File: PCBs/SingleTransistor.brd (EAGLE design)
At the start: 16 x 33 mm, 4 parts, among them T1 BC547N

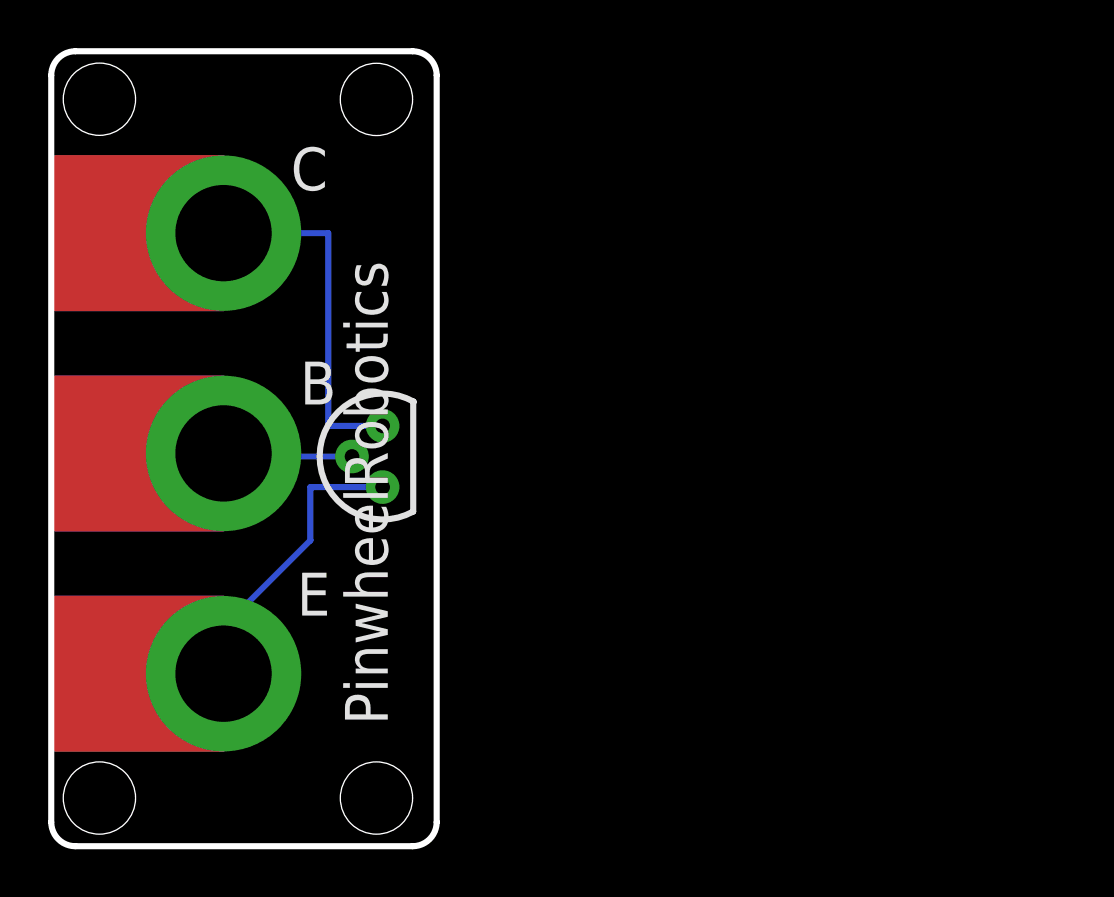
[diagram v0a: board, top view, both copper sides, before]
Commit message: Update for Dim width is 42 length is 28 for type 2 pcb
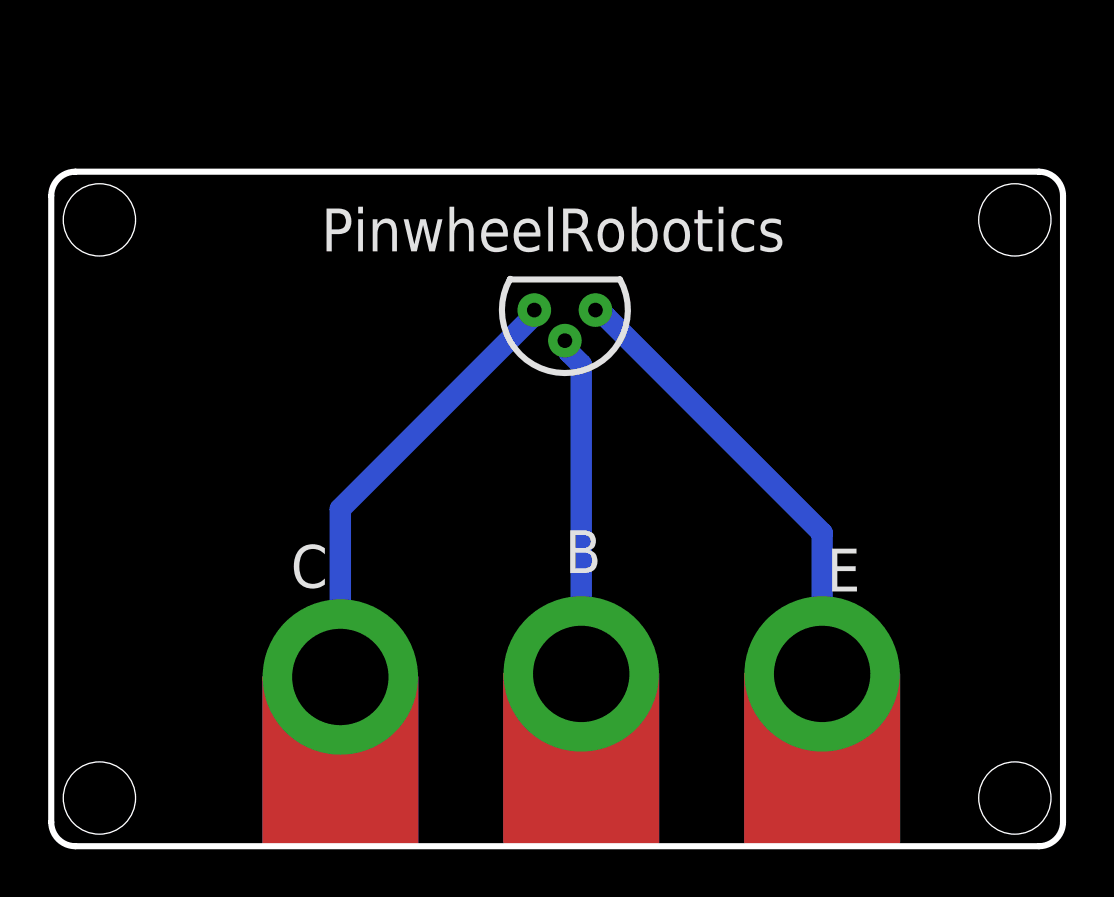
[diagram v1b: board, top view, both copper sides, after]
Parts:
- moved U$3 24.8 mm to (32.0, 7.15), turned to 0 degrees
- moved U$1 19.1 mm to (12.0, 7.03), turned to 0 degrees
- moved U$2 17.4 mm to (22.0, 7.15), turned to 0 degrees
- moved T1 11.5 mm to (22.6, 22.3), turned to 180 degrees
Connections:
- net N$2 renamed T1
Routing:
- net T1: track 5.46 -> 14.1 mm
- net N$1: track 12.7 -> 19.1 mm
- net N$3: track 14.6 -> 18.5 mm
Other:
- board size 16 x 33 mm -> 42 x 28 mm
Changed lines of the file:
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@@
 <drawing>
 <settings>
-<setting alwaysvectorfont="no"/>
+<setting alwaysvectorfont="yes"/>
 <setting verticaltext="up"/>
 </settings>
@@
 <layer number="45" name="Holes" color="7" fill="1" visible="yes" active="yes"/>
 <layer number="46" name="Milling" color="3" fill="1" visible="no" active="yes"/>
-<layer number="47" name="Measures" color="7" fill="1" visible="no" active="yes"/>
+<layer number="47" name="Measures" color="7" fill="1" visible="yes" active="yes"/>
 <layer number="48" name="Document" color="7" fill="1" visible="yes" active="yes"/>
 <layer number="49" name="Reference" color="7" fill="1" visible="yes" active="yes"/>
@@
 <board>
 <plain>
-<text x="10.2" y="9.574" size="1.778" layer="21">E</text>
-<text x="10.327" y="18.337" size="1.778" layer="21">B</text>
-<text x="9.946" y="27.227" size="1.778" layer="21">C</text>
-<hole x="2" y="31.008" drill="3"/>
-<hole x="13.5" y="31" drill="3"/>
-<hole x="13.5" y="2" drill="3"/>
+<text x="32.2" y="10.574" size="1.778" layer="21">E</text>
+<text x="21.327" y="11.337" size="1.778" layer="21">B</text>
+<text x="9.946" y="10.727" size="1.778" layer="21">C</text>
+<hole x="2" y="26" drill="3"/>
+<hole x="40" y="26" drill="3"/>
+<hole x="40" y="2" drill="3"/>
 <hole x="2" y="2" drill="3"/>
-<text x="13.971" y="5.042" size="1.778" layer="21" rot="R90">PinwheelRobotics</text>
-<text x="4.471" y="25.465" size="1.778" layer="22" rot="MR270">care@pinwheel.in</text>
-<wire x1="0" y1="1" x2="0" y2="32" width="0.254" layer="20"/>
-<wire x1="0" y1="32" x2="1" y2="33" width="0.254" layer="20" curve="-90"/>
-<wire x1="1" y1="33" x2="15" y2="33" width="0.254" layer="20"/>
-<wire x1="15" y1="33" x2="16" y2="32" width="0.254" layer="20" curve="-90"/>
-<wire x1="16" y1="32" x2="16" y2="1" width="0.254" layer="20"/>
-<wire x1="16" y1="1" x2="15" y2="0" width="0.254" layer="20" curve="-90"/>
-<wire x1="15" y1="0" x2="1" y2="0" width="0.254" layer="20"/>
+<text x="30.458" y="26.471" size="1.778" layer="21" rot="R180">PinwheelRobotics</text>
+<text x="10.535" y="26.471" size="1.778" layer="22" rot="MR180">care@pinwheel.in</text>
+<wire x1="42" y1="27" x2="42" y2="1" width="0.254" layer="20"/>
+<wire x1="42" y1="1" x2="41" y2="0" width="0.254" layer="20" curve="-90"/>
+<wire x1="41" y1="0" x2="1" y2="0" width="0.254" layer="20"/>
 <wire x1="1" y1="0" x2="0" y2="1" width="0.254" layer="20" curve="-90"/>
-<dimension x1="-1.5" y1="33" x2="-1.5" y2="0" x3="-2.5" y3="16.5" textsize="1.778" layer="1"/>
-<dimension x1="0" y1="33.5" x2="16" y2="33.5" x3="8" y3="35.5" textsize="1.778" layer="1"/>
+<wire x1="0" y1="1" x2="0" y2="27" width="0.254" layer="20"/>
+<wire x1="0" y1="27" x2="1" y2="28" width="0.254" layer="20" curve="-90"/>
+<wire x1="1" y1="28" x2="41" y2="28" width="0.254" layer="20"/>
+<wire x1="41" y1="28" x2="42" y2="27" width="0.254" layer="20" curve="-90"/>
 </plain>
 <attributes>
@@
 </class>
 </classes>
-<designrules name="default">
+<designrules name="default *">
 <description language="de">&lt;b&gt;EAGLE Design Rules&lt;/b&gt;
 &lt;p&gt;
@@
 <param name="mdDrill" value="6mil"/>
 <param name="mdSmdStop" value="0mil"/>
-<param name="msWidth" value="6mil"/>
+<param name="msWidth" value="35mil"/>
 <param name="msDrill" value="0.35mm"/>
 <param name="msMicroVia" value="9.99mm"/>
@@
 <param name="TopRouterVariant" value="1"/>
 <param name="tpViaShape" value="round"/>
-<param name="PrefDir.1" value="0"/>
+<param name="PrefDir.1" value="a"/>
 <param name="PrefDir.2" value="0"/>
 <param name="PrefDir.3" value="0"/>
@@
 </autorouter>
 <elements>
-<element name="T1" library="BC547" package="TO92" value="BC547N" x="13.756" y="14.908" smashed="yes" rot="R90">
-<attribute name="AVAILABILITY" value="In Stock" x="16.296" y="37.768" size="1.778" layer="27" rot="R90" display="off"/>
-<attribute name="CHECK_PRICES" value="https://www.snapeda.com/parts/BC547/Onsemi/view-part/?ref=eda" x="16.296" y="37.768" size="1.778" layer="27" rot="R90" display="off"/>
-<attribute name="DESCRIPTION" value=" Trans GP BJT NPN 45V 0.1A 500mW 3-Pin TO-92 T/R " x="16.296" y="37.768" size="1.778" layer="27" rot="R90" display="off"/>
-<attribute name="MF" value="ON Semiconductor" x="16.296" y="37.768" size="1.778" layer="27" rot="R90" display="off"/>
-<attribute name="MP" value="BC547" x="16.296" y="37.768" size="1.778" layer="27" rot="R90" display="off"/>
-<attribute name="PACKAGE" value="None" x="16.296" y="37.768" size="1.778" layer="27" rot="R90" display="off"/>
-<attribute name="PRICE" value="None" x="16.296" y="37.768" size="1.778" layer="27" rot="R90" display="off"/>
-<attribute name="PURCHASE-URL" value="https://www.snapeda.com/api/url_track_click_mouser/?unipart_id=11254981&amp;manufacturer=ON Semiconductor&amp;part_name=BC547&amp;search_term=None" x="16.296" y="37.768" size="1.778" layer="27" rot="R90" display="off"/>
-<attribute name="SNAPEDA_LINK" value="https://www.snapeda.com/parts/BC547/Onsemi/view-part/?ref=snap" x="16.296" y="37.768" size="1.778" layer="27" rot="R90" display="off"/>
-<attribute name="VALUE" x="10.962" y="18.337" size="0.8128" layer="27" rot="R270"/>
+<element name="T1" library="BC547" package="TO92" value="BC547N" x="22.592" y="22.256" smashed="yes" rot="R180">
+<attribute name="AVAILABILITY" value="In Stock" x="-0.268" y="24.796" size="1.778" layer="27" rot="R180" display="off"/>
+<attribute name="CHECK_PRICES" value="https://www.snapeda.com/parts/BC547/Onsemi/view-part/?ref=eda" x="-0.268" y="24.796" size="1.778" layer="27" rot="R180" display="off"/>
+<attribute name="DESCRIPTION" value=" Trans GP BJT NPN 45V 0.1A 500mW 3-Pin TO-92 T/R " x="-0.268" y="24.796" size="1.778" layer="27" rot="R180" display="off"/>
+<attribute name="MF" value="ON Semiconductor" x="-0.268" y="24.796" size="1.778" layer="27" rot="R180" display="off"/>
+<attribute name="MP" value="BC547" x="-0.268" y="24.796" size="1.778" layer="27" rot="R180" display="off"/>
+<attribute name="PACKAGE" value="None" x="-0.268" y="24.796" size="1.778" layer="27" rot="R180" display="off"/>
+<attribute name="PRICE" value="None" x="-0.268" y="24.796" size="1.778" layer="27" rot="R180" display="off"/>
+<attribute name="PURCHASE-URL" value="https://www.snapeda.com/api/url_track_click_mouser/?unipart_id=11254981&amp;manufacturer=ON Semiconductor&amp;part_name=BC547&amp;search_term=None" x="-0.268" y="24.796" size="1.778" layer="27" rot="R180" display="off"/>
+<attribute name="SNAPEDA_LINK" value="https://www.snapeda.com/parts/BC547/Onsemi/view-part/?ref=snap" x="-0.268" y="24.796" size="1.778" layer="27" rot="R180" display="off"/>
+<attribute name="VALUE" x="19.663" y="18.462" size="0.8128" layer="27"/>
 </element>
-<element name="U$1" library="microbit" package="MICROBIT_PAD" value="MICROBIT_PAD" x="7.152" y="25.449" smashed="yes" rot="R270"/>
-<element name="U$2" library="microbit" package="MICROBIT_PAD" value="MICROBIT_PAD" x="7.152" y="16.305" smashed="yes" rot="R270"/>
-<element name="U$3" library="microbit" package="MICROBIT_PAD" value="MICROBIT_PAD" x="7.152" y="7.161" smashed="yes" rot="R270"/>
+<element name="U$1" library="microbit" package="MICROBIT_PAD" value="MICROBIT_PAD" x="12" y="7.025" smashed="yes"/>
+<element name="U$2" library="microbit" package="MICROBIT_PAD" value="MICROBIT_PAD" x="22" y="7.152" smashed="yes"/>
+<element name="U$3" library="microbit" package="MICROBIT_PAD" value="MICROBIT_PAD" x="32" y="7.152" smashed="yes"/>
 </elements>
 <signals>
@@
 <contactref element="U$3" pad="PAD"/>
 <contactref element="T1" pad="1"/>
-<wire x1="13.756" y1="14.908" x2="10.7588" y2="14.908" width="0.254" layer="16"/>
-<wire x1="7.152" y1="9.8661" x2="7.152" y2="7.161" width="0.254" layer="16"/>
-<wire x1="10.7588" y1="14.908" x2="10.7588" y2="12.6982" width="0.254" layer="16"/>
-<wire x1="10.7588" y1="12.6982" x2="7.9267" y2="9.8661" width="0.254" layer="16"/>
-<wire x1="7.9267" y1="9.8661" x2="7.152" y2="9.8661" width="0.254" layer="16"/>
+<wire x1="32" y1="13" x2="23" y2="22" width="0.889" layer="16"/>
+<wire x1="32" y1="7.152" x2="32" y2="13" width="0.889" layer="16"/>
+<wire x1="23" y1="22" x2="22.592" y2="22.256" width="0.889" layer="16"/>
 </signal>
-<signal name="N$2">
+<signal name="T1">
 <contactref element="T1" pad="2"/>
 <contactref element="U$2" pad="PAD"/>
-<wire x1="12.486" y1="16.178" x2="7.152" y2="16.178" width="0.254" layer="16"/>
-<wire x1="7.152" y1="16.178" x2="7.152" y2="16.305" width="0.254" layer="16"/>
+<wire x1="22" y1="20" x2="21.5" y2="20.5" width="0.889" layer="16"/>
+<wire x1="22" y1="7.152" x2="22" y2="20" width="0.889" layer="16"/>
+<wire x1="21.5" y1="20.5" x2="21.322" y2="20.986" width="0.889" layer="16"/>
 </signal>
 <signal name="N$3">
 <contactref element="T1" pad="3"/>
 <contactref element="U$1" pad="PAD"/>
-<wire x1="7.152" y1="25.449" x2="11.5" y2="25.449" width="0.254" layer="16"/>
-<wire x1="11.5" y1="17.448" x2="13.756" y2="17.448" width="0.254" layer="16"/>
-<wire x1="11.5" y1="25.449" x2="11.5" y2="17.448" width="0.254" layer="16"/>
+<wire x1="12" y1="14" x2="20" y2="22" width="0.889" layer="16"/>
+<wire x1="12" y1="7.025" x2="12" y2="14" width="0.889" layer="16"/>
+<wire x1="20" y1="22" x2="20.052" y2="22.256" width="0.889" layer="16"/>
 </signal>
 </signals>
@@
 <mfgpreviewcolor name="substratecolor" color="0xFF786E46"/>
 </mfgpreviewcolors>
-<errors>
-</errors>
 </board>
 </drawing>

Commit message: Corrected hole position for some design , made transistor as switch as category 1
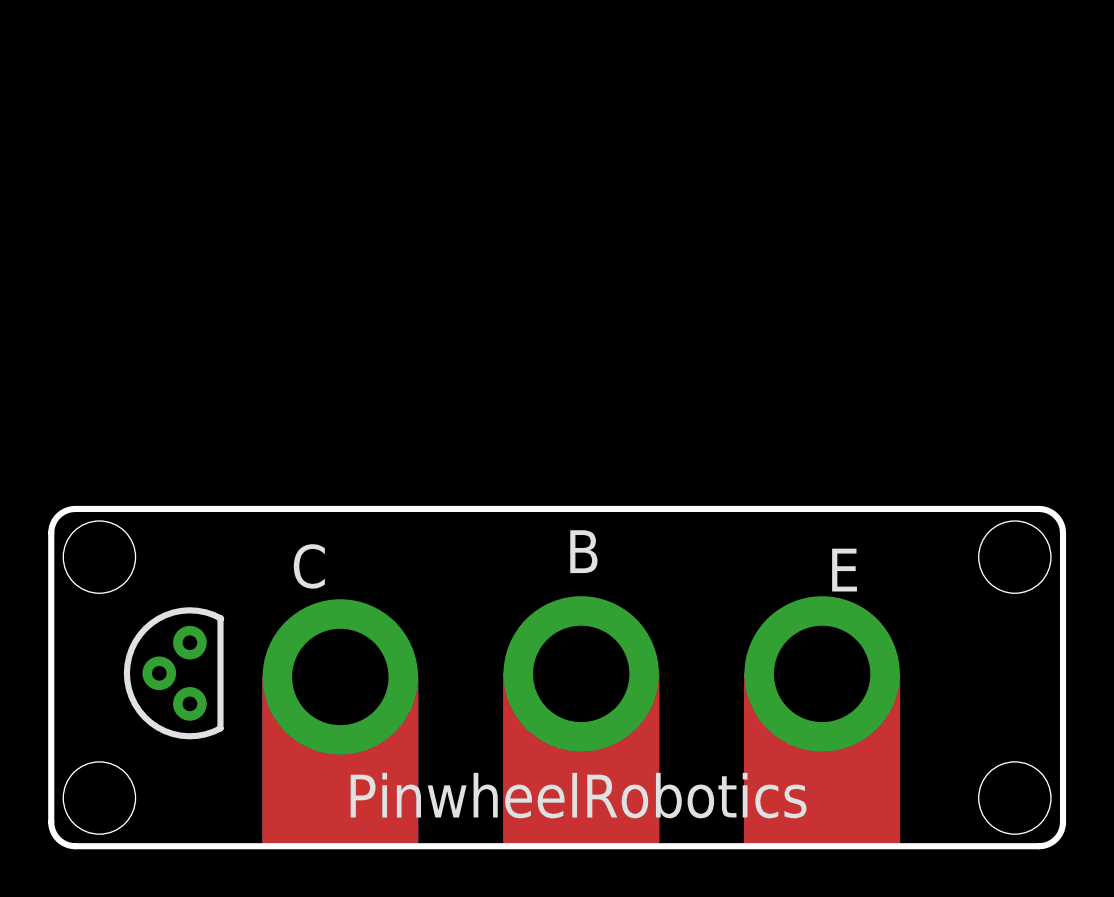
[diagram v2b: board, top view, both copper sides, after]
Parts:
- moved T1 23.5 mm to (5.76, 5.91), turned to 90 degrees
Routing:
- net N$1: track 19.1 -> 0.00 mm
- net N$3: track 18.5 -> 0.00 mm
- net T1: track 14.1 -> 0.00 mm
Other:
- board size 42 x 28 mm -> 42 x 14 mm
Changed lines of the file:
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@@
 <drawing>
 <settings>
-<setting alwaysvectorfont="yes"/>
+<setting alwaysvectorfont="no"/>
 <setting verticaltext="up"/>
 </settings>
@@
 <text x="21.327" y="11.337" size="1.778" layer="21">B</text>
 <text x="9.946" y="10.727" size="1.778" layer="21">C</text>
-<hole x="2" y="26" drill="3"/>
-<hole x="40" y="26" drill="3"/>
+<hole x="2" y="12" drill="3"/>
+<hole x="40" y="12" drill="3"/>
 <hole x="40" y="2" drill="3"/>
 <hole x="2" y="2" drill="3"/>
-<text x="30.458" y="26.471" size="1.778" layer="21" rot="R180">PinwheelRobotics</text>
-<text x="10.535" y="26.471" size="1.778" layer="22" rot="MR180">care@pinwheel.in</text>
-<wire x1="42" y1="27" x2="42" y2="1" width="0.254" layer="20"/>
+<text x="31.458" y="2.971" size="1.778" layer="21" rot="R180">PinwheelRobotics</text>
+<text x="11.535" y="13.471" size="1.778" layer="22" rot="MR180">care@pinwheel.in</text>
+<wire x1="42" y1="13" x2="42" y2="1" width="0.254" layer="20"/>
 <wire x1="42" y1="1" x2="41" y2="0" width="0.254" layer="20" curve="-90"/>
 <wire x1="41" y1="0" x2="1" y2="0" width="0.254" layer="20"/>
 <wire x1="1" y1="0" x2="0" y2="1" width="0.254" layer="20" curve="-90"/>
-<wire x1="0" y1="1" x2="0" y2="27" width="0.254" layer="20"/>
-<wire x1="0" y1="27" x2="1" y2="28" width="0.254" layer="20" curve="-90"/>
-<wire x1="1" y1="28" x2="41" y2="28" width="0.254" layer="20"/>
-<wire x1="41" y1="28" x2="42" y2="27" width="0.254" layer="20" curve="-90"/>
+<wire x1="0" y1="1" x2="0" y2="13" width="0.254" layer="20"/>
+<wire x1="0" y1="13" x2="1" y2="14" width="0.254" layer="20" curve="-90"/>
+<wire x1="1" y1="14" x2="41" y2="14" width="0.254" layer="20"/>
+<wire x1="41" y1="14" x2="42" y2="13" width="0.254" layer="20" curve="-90"/>
 </plain>
 <attributes>
@@
 </autorouter>
 <elements>
-<element name="T1" library="BC547" package="TO92" value="BC547N" x="22.592" y="22.256" smashed="yes" rot="R180">
-<attribute name="AVAILABILITY" value="In Stock" x="-0.268" y="24.796" size="1.778" layer="27" rot="R180" display="off"/>
-<attribute name="CHECK_PRICES" value="https://www.snapeda.com/parts/BC547/Onsemi/view-part/?ref=eda" x="-0.268" y="24.796" size="1.778" layer="27" rot="R180" display="off"/>
-<attribute name="DESCRIPTION" value=" Trans GP BJT NPN 45V 0.1A 500mW 3-Pin TO-92 T/R " x="-0.268" y="24.796" size="1.778" layer="27" rot="R180" display="off"/>
-<attribute name="MF" value="ON Semiconductor" x="-0.268" y="24.796" size="1.778" layer="27" rot="R180" display="off"/>
-<attribute name="MP" value="BC547" x="-0.268" y="24.796" size="1.778" layer="27" rot="R180" display="off"/>
-<attribute name="PACKAGE" value="None" x="-0.268" y="24.796" size="1.778" layer="27" rot="R180" display="off"/>
-<attribute name="PRICE" value="None" x="-0.268" y="24.796" size="1.778" layer="27" rot="R180" display="off"/>
-<attribute name="PURCHASE-URL" value="https://www.snapeda.com/api/url_track_click_mouser/?unipart_id=11254981&amp;manufacturer=ON Semiconductor&amp;part_name=BC547&amp;search_term=None" x="-0.268" y="24.796" size="1.778" layer="27" rot="R180" display="off"/>
-<attribute name="SNAPEDA_LINK" value="https://www.snapeda.com/parts/BC547/Onsemi/view-part/?ref=snap" x="-0.268" y="24.796" size="1.778" layer="27" rot="R180" display="off"/>
-<attribute name="VALUE" x="19.663" y="18.462" size="0.8128" layer="27"/>
+<element name="T1" library="BC547" package="TO92" value="BC547N" x="5.756" y="5.908" smashed="yes" rot="R90">
+<attribute name="AVAILABILITY" value="In Stock" x="8.296" y="28.768" size="1.778" layer="27" rot="R90" display="off"/>
+<attribute name="CHECK_PRICES" value="https://www.snapeda.com/parts/BC547/Onsemi/view-part/?ref=eda" x="8.296" y="28.768" size="1.778" layer="27" rot="R90" display="off"/>
+<attribute name="DESCRIPTION" value=" Trans GP BJT NPN 45V 0.1A 500mW 3-Pin TO-92 T/R " x="8.296" y="28.768" size="1.778" layer="27" rot="R90" display="off"/>
+<attribute name="MF" value="ON Semiconductor" x="8.296" y="28.768" size="1.778" layer="27" rot="R90" display="off"/>
+<attribute name="MP" value="BC547" x="8.296" y="28.768" size="1.778" layer="27" rot="R90" display="off"/>
+<attribute name="PACKAGE" value="None" x="8.296" y="28.768" size="1.778" layer="27" rot="R90" display="off"/>
+<attribute name="PRICE" value="None" x="8.296" y="28.768" size="1.778" layer="27" rot="R90" display="off"/>
+<attribute name="PURCHASE-URL" value="https://www.snapeda.com/api/url_track_click_mouser/?unipart_id=11254981&amp;manufacturer=ON Semiconductor&amp;part_name=BC547&amp;search_term=None" x="8.296" y="28.768" size="1.778" layer="27" rot="R90" display="off"/>
+<attribute name="SNAPEDA_LINK" value="https://www.snapeda.com/parts/BC547/Onsemi/view-part/?ref=snap" x="8.296" y="28.768" size="1.778" layer="27" rot="R90" display="off"/>
+<attribute name="VALUE" x="1.962" y="8.837" size="0.8128" layer="27" rot="R270"/>
 </element>
 <element name="U$1" library="microbit" package="MICROBIT_PAD" value="MICROBIT_PAD" x="12" y="7.025" smashed="yes"/>
@@
 <contactref element="U$3" pad="PAD"/>
 <contactref element="T1" pad="1"/>
-<wire x1="32" y1="13" x2="23" y2="22" width="0.889" layer="16"/>
-<wire x1="32" y1="7.152" x2="32" y2="13" width="0.889" layer="16"/>
-<wire x1="23" y1="22" x2="22.592" y2="22.256" width="0.889" layer="16"/>
+<wire x1="5.756" y1="5.908" x2="32" y2="7.152" width="0" layer="19" extent="1-1"/>
 </signal>
 <signal name="T1">
 <contactref element="T1" pad="2"/>
 <contactref element="U$2" pad="PAD"/>
-<wire x1="22" y1="20" x2="21.5" y2="20.5" width="0.889" layer="16"/>
-<wire x1="22" y1="7.152" x2="22" y2="20" width="0.889" layer="16"/>
-<wire x1="21.5" y1="20.5" x2="21.322" y2="20.986" width="0.889" layer="16"/>
+<wire x1="4.486" y1="7.178" x2="22" y2="7.152" width="0" layer="19" extent="1-1"/>
 </signal>
 <signal name="N$3">
 <contactref element="T1" pad="3"/>
 <contactref element="U$1" pad="PAD"/>
-<wire x1="12" y1="14" x2="20" y2="22" width="0.889" layer="16"/>
-<wire x1="12" y1="7.025" x2="12" y2="14" width="0.889" layer="16"/>
-<wire x1="20" y1="22" x2="20.052" y2="22.256" width="0.889" layer="16"/>
+<wire x1="5.756" y1="8.448" x2="12" y2="7.025" width="0" layer="19" extent="1-1"/>
 </signal>
 </signals>
